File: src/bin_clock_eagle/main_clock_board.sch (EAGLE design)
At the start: 79 parts, among them Q2 16mhz, U1 ATMEGA328P-AU

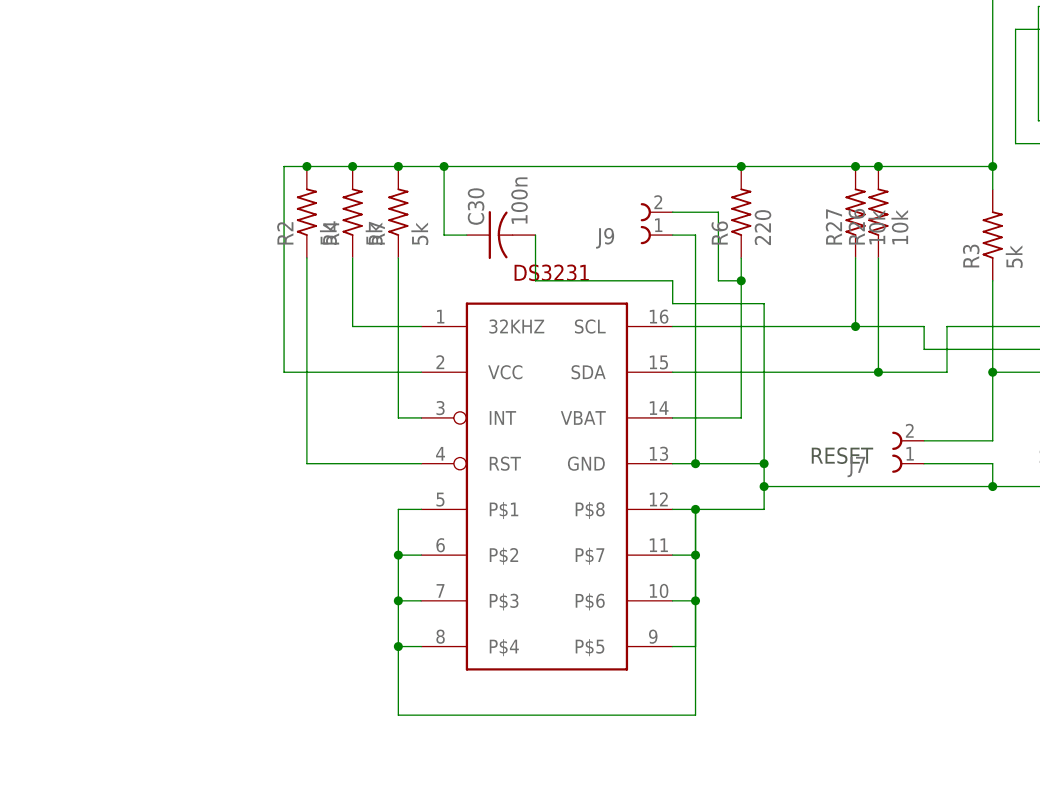
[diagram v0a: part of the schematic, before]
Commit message: fixed ds3231 package to SO16W
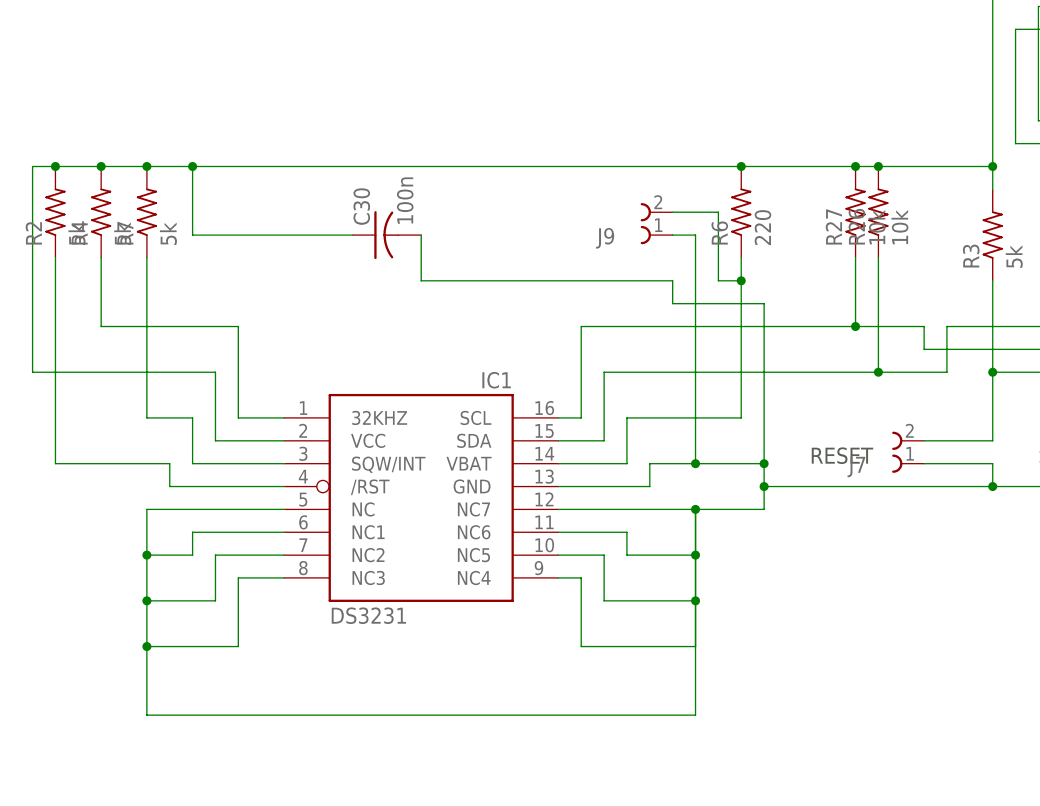
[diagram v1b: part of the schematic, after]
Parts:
- removed U$1: DS3231, DS3231:DS3231
- added IC1: DS3231/SO, DS3231_so16w:DS3231/SO
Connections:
- net GND: now also IC1.GND, IC1.NC, IC1.NC1, IC1.NC2, IC1.NC3, IC1.NC4, IC1.NC5, IC1.NC6, IC1.NC7; no longer U$1.GND, U$1.P$1, U$1.P$2, U$1.P$3, U$1.P$4, U$1.P$5, U$1.P$6, U$1.P$7, U$1.P$8
- net N$10: now also IC1.SCL; no longer U$1.SCL
- net N$15: now also IC1./RST; no longer U$1.RST
- net N$2: now also IC1.SDA; no longer U$1.SDA
- net N$43: now also IC1.32KHZ; no longer U$1.32KHZ
- net N$44: now also IC1.VBAT; no longer U$1.VBAT
- net N$45: now also IC1.SQW/INT; no longer U$1.INT
- net VCC: now also IC1.VCC; no longer U$1.VCC
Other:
- moved on the sheet: C30, R2, R4, R7
